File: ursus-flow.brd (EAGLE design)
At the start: 90.2 x 50.8 mm, 61 parts

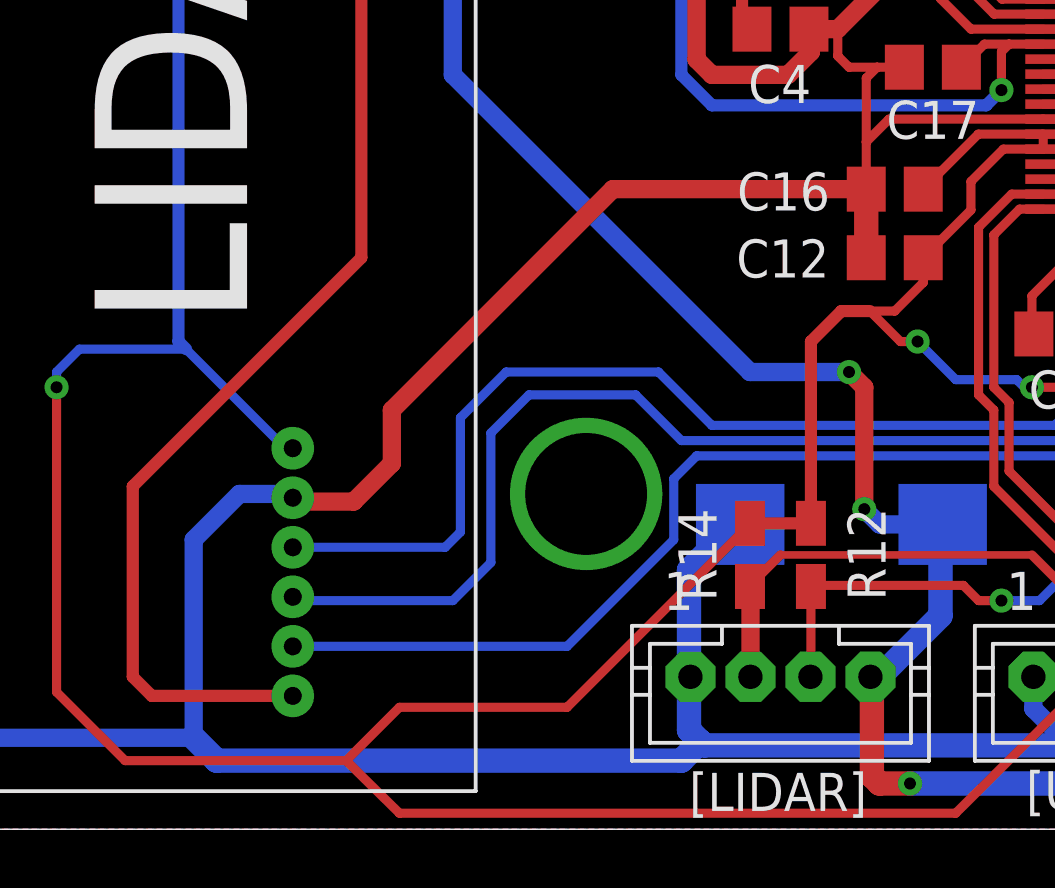
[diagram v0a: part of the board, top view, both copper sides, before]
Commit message: Adjust MPU9250 drill size
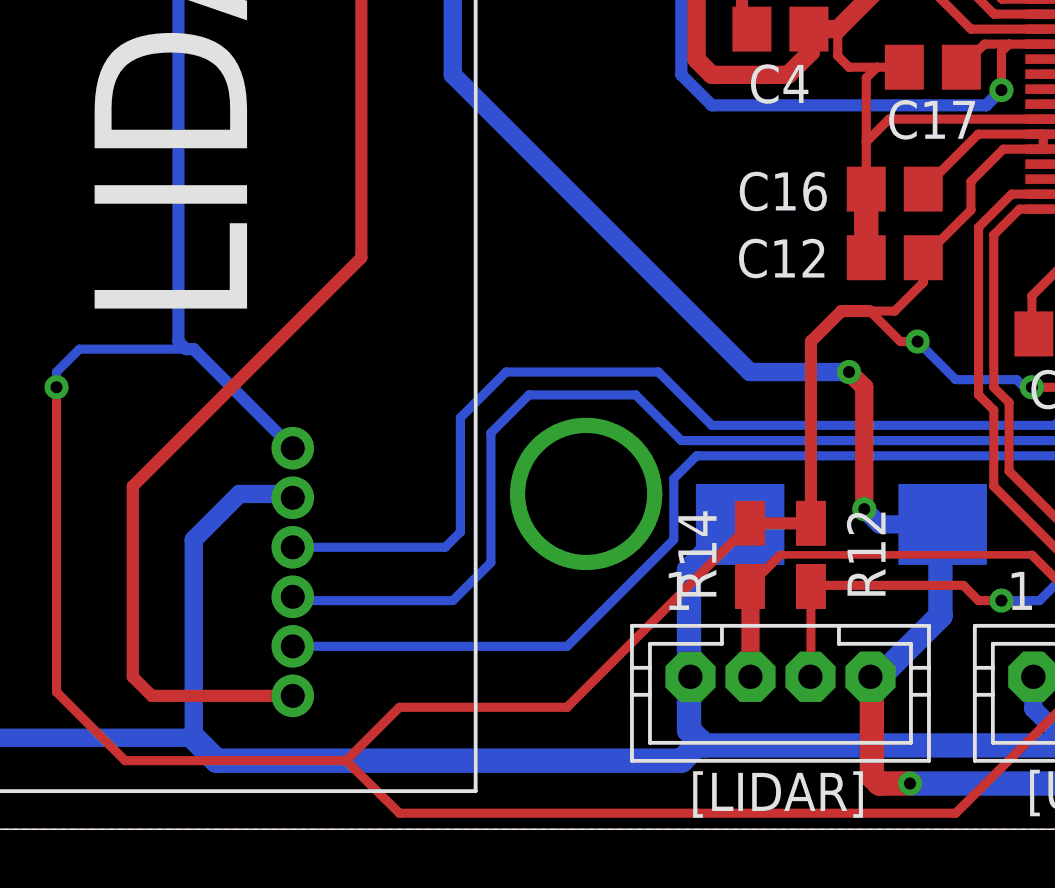
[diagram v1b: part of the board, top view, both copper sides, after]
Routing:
- net GND: track 478.6 -> 454.0 mm
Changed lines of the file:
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@@
 <layer number="21" name="tPlace" color="7" fill="1" visible="yes" active="yes"/>
 <layer number="22" name="bPlace" color="7" fill="1" visible="yes" active="yes"/>
-<layer number="23" name="tOrigins" color="15" fill="1" visible="no" active="yes"/>
-<layer number="24" name="bOrigins" color="15" fill="1" visible="no" active="yes"/>
+<layer number="23" name="tOrigins" color="15" fill="1" visible="yes" active="yes"/>
+<layer number="24" name="bOrigins" color="15" fill="1" visible="yes" active="yes"/>
 <layer number="25" name="tNames" color="7" fill="1" visible="yes" active="yes"/>
 <layer number="26" name="bNames" color="7" fill="1" visible="yes" active="yes"/>
@@
 <wire x1="47.8" y1="34.29" x2="47.8" y2="33.226" width="0.6096" layer="16"/>
 <wire x1="47.8" y1="33.226" x2="49.022" y2="32.004" width="0.6096" layer="16"/>
-<wire x1="42.23" y1="50.546" x2="33.782" y2="50.546" width="0.6096" layer="1"/>
-<wire x1="33.782" y1="50.546" x2="26.416" y2="43.18" width="0.6096" layer="1"/>
-<wire x1="26.416" y1="43.18" x2="26.416" y2="41.402" width="0.6096" layer="1"/>
-<wire x1="26.416" y1="41.402" x2="25.146" y2="40.132" width="0.6096" layer="1"/>
 <wire x1="63.63" y1="61.38" x2="62.826" y2="61.38" width="0.3048" layer="1"/>
 <wire x1="62.826" y1="61.38" x2="62.23" y2="61.976" width="0.3048" layer="1"/>
@@
 <wire x1="66.294" y1="63.18" x2="68.072" y2="63.18" width="0.3048" layer="1"/>
 <wire x1="68.072" y1="63.18" x2="68.326" y2="63.434" width="0.3048" layer="1"/>
-<contactref element="U$11" pad="P$2"/>
-<wire x1="25.146" y1="40.132" x2="23.114" y2="40.132" width="0.6096" layer="1"/>
-<wire x1="23.114" y1="40.132" x2="23.114" y2="40.259" width="0.6096" layer="1"/>
 <wire x1="19.812" y1="32.258" x2="19.812" y2="38.862" width="0.6096" layer="16"/>
 <wire x1="19.812" y1="38.862" x2="21.336" y2="40.386" width="0.6096" layer="16"/>
-<wire x1="21.336" y1="40.386" x2="22.987" y2="40.386" width="0.6096" layer="16"/>
-<wire x1="22.987" y1="40.386" x2="23.114" y2="40.259" width="0.6096" layer="16"/>
 <wire x1="42.23" y1="50.546" x2="42.23" y2="52.1208" width="0.3048" layer="1"/>
 <wire x1="42.23" y1="52.1208" x2="42.23" y2="54.24928125" width="0.3048" layer="1"/>
@@
 <wire x1="42.9892" y1="52.88" x2="42.23" y2="52.1208" width="0.3048" layer="1"/>
 <wire x1="49.53" y1="52.88" x2="49.88" y2="52.53" width="0.3048" layer="1"/>
+<contactref element="U$11" pad="P$2"/>
+<wire x1="21.336" y1="40.386" x2="22.987" y2="40.386" width="0.6096" layer="16"/>
+<wire x1="22.987" y1="40.386" x2="23.114" y2="40.259" width="0.6096" layer="16"/>
+<wire x1="57.912" y1="53.086" x2="57.912" y2="54.356" width="0" layer="19" extent="1-16"/>
+<wire x1="16.155" y1="64.77" x2="16.51" y2="64.77" width="0" layer="19" extent="16-16"/>
 </signal>
 <signal name="+5V">
@@
 <wire x1="64.262" y1="62.738" x2="64.262" y2="63.18" width="0.3048" layer="1"/>
 <wire x1="64.262" y1="63.18" x2="64.328" y2="63.246" width="0.3048" layer="1"/>
-<contactref element="U$11" pad="P$1"/>
-<wire x1="23.114" y1="41.91" x2="22.86" y2="41.91" width="0.3048" layer="16"/>
-<wire x1="22.86" y1="41.91" x2="19.558" y2="45.212" width="0.3048" layer="16"/>
 <wire x1="44.13" y1="48.26" x2="44.13" y2="47.432" width="0.3048" layer="1"/>
 <wire x1="44.13" y1="47.432" x2="43.18" y2="46.482" width="0.3048" layer="1"/>
@@
 <wire x1="16.4846" y1="68.5546" x2="16.5354" y2="68.5546" width="0.8128" layer="16"/>
 <wire x1="16.5354" y1="68.5546" x2="19.405" y2="65.685" width="0.8128" layer="16"/>
+<wire x1="19.558" y1="45.212" x2="19.812" y2="45.212" width="0.4064" layer="16"/>
+<contactref element="U$11" pad="P$1"/>
+<wire x1="23.114" y1="41.91" x2="19.812" y2="45.212" width="0.4064" layer="16"/>
 </signal>
 <signal name="USB_OTG_FS_DP">
@@
 <wire x1="29.718" y1="38.1" x2="28.448" y2="36.83" width="0.3048" layer="16"/>
 <wire x1="36.068" y1="42.164" x2="51.308" y2="42.164" width="0.3048" layer="16"/>
+<wire x1="28.448" y1="36.83" x2="23.114" y2="36.83" width="0.3048" layer="16"/>
 <contactref element="U$11" pad="P$4"/>
-<wire x1="28.448" y1="36.83" x2="23.114" y2="36.83" width="0.3048" layer="16"/>
-<wire x1="23.114" y1="36.83" x2="23.114" y2="36.957" width="0.3048" layer="16"/>
+<wire x1="23.114" y1="36.957" x2="23.114" y2="36.83" width="0" layer="19" extent="16-16"/>
 </signal>
 <signal name="MPU9250_SPI1_MOSI">

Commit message: Do circuit final check
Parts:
- removed C19: 100uf/10V, rcl:B/3528-21W
- added C18: 100uf/10V, rcl:C/6032-28R
- renumbered U$10 to U$14, U$7 to U$13, U$8 to U$15, U$9 to U$12
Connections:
- net +5V: now also C18.+; no longer C19.+
- net GND: now also C18.-; no longer C19.-, U$3.CASING3, U$3.CASING4
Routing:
- net GND: track 454.0 -> 468.5 mm, vias 4 -> 5
- net +5V: track 150.0 -> 147.0 mm, vias 5 -> 4
